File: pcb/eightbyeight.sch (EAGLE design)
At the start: 163 parts, among them J1 USB_MICROSMT+THRUHULE, J2 BATTERY, Q1 16MHz, SW1 SWITCH_SPDT, SW2 BRIGHTNESS, U1 MK20DN64VFM5, U10 FDG6316P, U11 FDG6316P, U12 FDG6316P, U2 ICN2026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

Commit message: Add HRC art
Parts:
- R28: value DNP -> 10k
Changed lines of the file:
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@@
 <part name="3V17" library="supply1" deviceset="+3V3" device=""/>
 <part name="3V18" library="supply1" deviceset="+3V3" device=""/>
-<part name="R28" library="adafruit" deviceset="R-US_" device="R0402" value="DNP"/>
+<part name="R28" library="adafruit" deviceset="R-US_" device="R0402" value="10k"/>
 <part name="3V1" library="supply1" deviceset="+3V3" device=""/>
 <part name="3V4" library="supply1" deviceset="+3V3" device=""/>
@@
 Revision E:
 -Implement more user friendly expansion pads for the ESP
+Revision F:
+-Round badge corners slightly
+-Increase base brightness for LED resistors
 TODO:
--Cosmetic: ESP8266 GPIO 18mislabeled, should be 16</text>
+-Cosmetic: ESP8266 GPIO 18mislabeled, should be 16
+-Clean silkscreen for final release</text>
 <text x="129.54" y="358.14" size="10.16" layer="91" align="bottom-center">EightByEight Blinky Badge</text>
 <text x="129.54" y="345.44" size="6.4516" layer="91" align="bottom-center">Copyright 2016 Blinkinlabs, LLC</text>

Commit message: Production silk and component values
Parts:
- R1: value 1.6k 1% -> 1k 1%
- R9: value 2k 1% -> 1k 1%
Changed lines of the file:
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@@
 <part name="GND2" library="SparkFun-Aesthetics" deviceset="GND" device=""/>
 <part name="C7" library="adafruit" deviceset="C-US" device="C0402" value="100nF"/>
-<part name="R1" library="adafruit" deviceset="R-US_" device="R0402" value="1.6k 1%"/>
+<part name="R1" library="adafruit" deviceset="R-US_" device="R0402" value="1k 1%"/>
 <part name="GND3" library="SparkFun-Aesthetics" deviceset="GND" device=""/>
 <part name="GND4" library="SparkFun-Aesthetics" deviceset="GND" device=""/>
@@
 <part name="U4" library="blinkinlabs" deviceset="ICN2026" device=""/>
 <part name="GND9" library="SparkFun-Aesthetics" deviceset="GND" device=""/>
-<part name="R9" library="adafruit" deviceset="R-US_" device="R0402" value="2k 1%"/>
+<part name="R9" library="adafruit" deviceset="R-US_" device="R0402" value="1k 1%"/>
 <part name="GND11" library="SparkFun-Aesthetics" deviceset="GND" device=""/>
 <part name="C11" library="adafruit" deviceset="C-US" device="C0402" value="100nF"/>
@@
 -Increase base brightness for LED resistors
 TODO:
--Cosmetic: ESP8266 GPIO 18mislabeled, should be 16
--Clean silkscreen for final release</text>
+-Cosmetic: ESP8266 GPIO 18mislabeled, should be 16</text>
 <text x="129.54" y="358.14" size="10.16" layer="91" align="bottom-center">EightByEight Blinky Badge</text>
 <text x="129.54" y="345.44" size="6.4516" layer="91" align="bottom-center">Copyright 2016 Blinkinlabs, LLC</text>

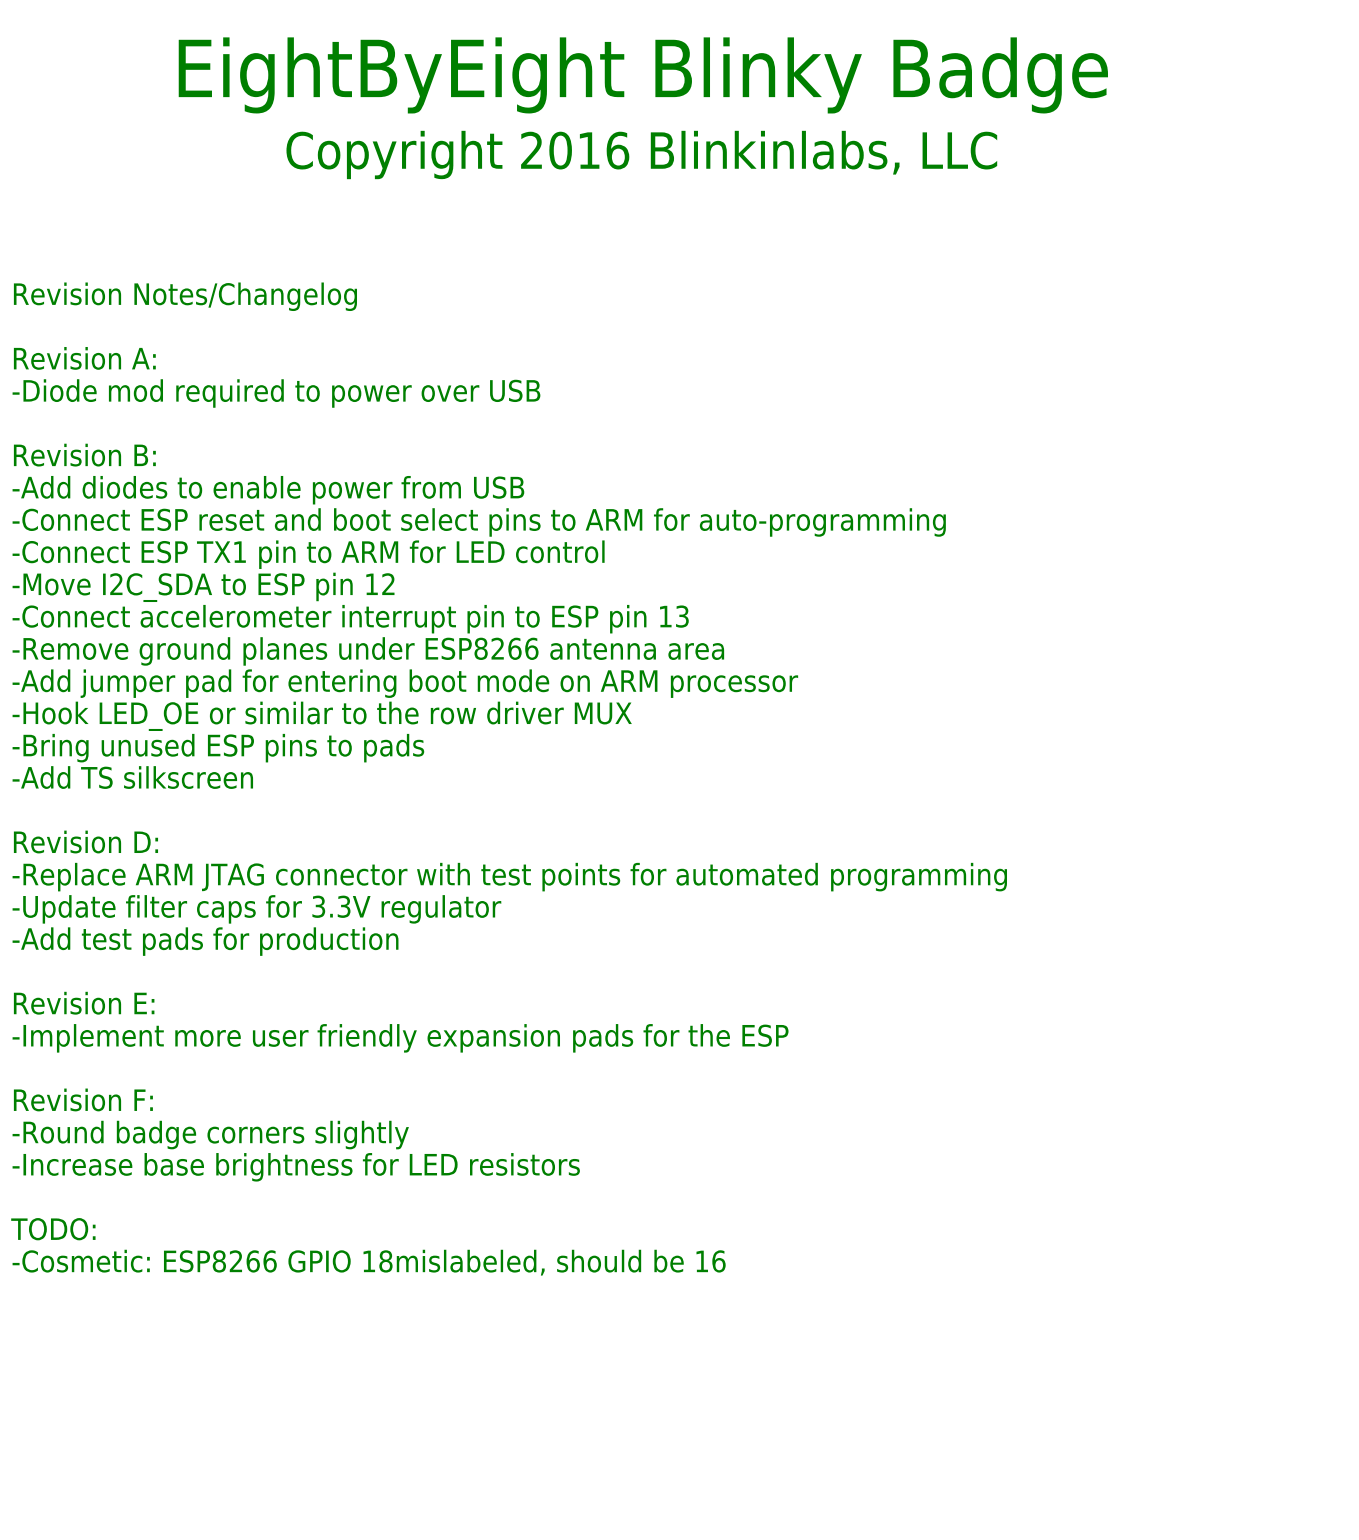
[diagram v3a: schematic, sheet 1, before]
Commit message: Add CERH OHL license to PCB
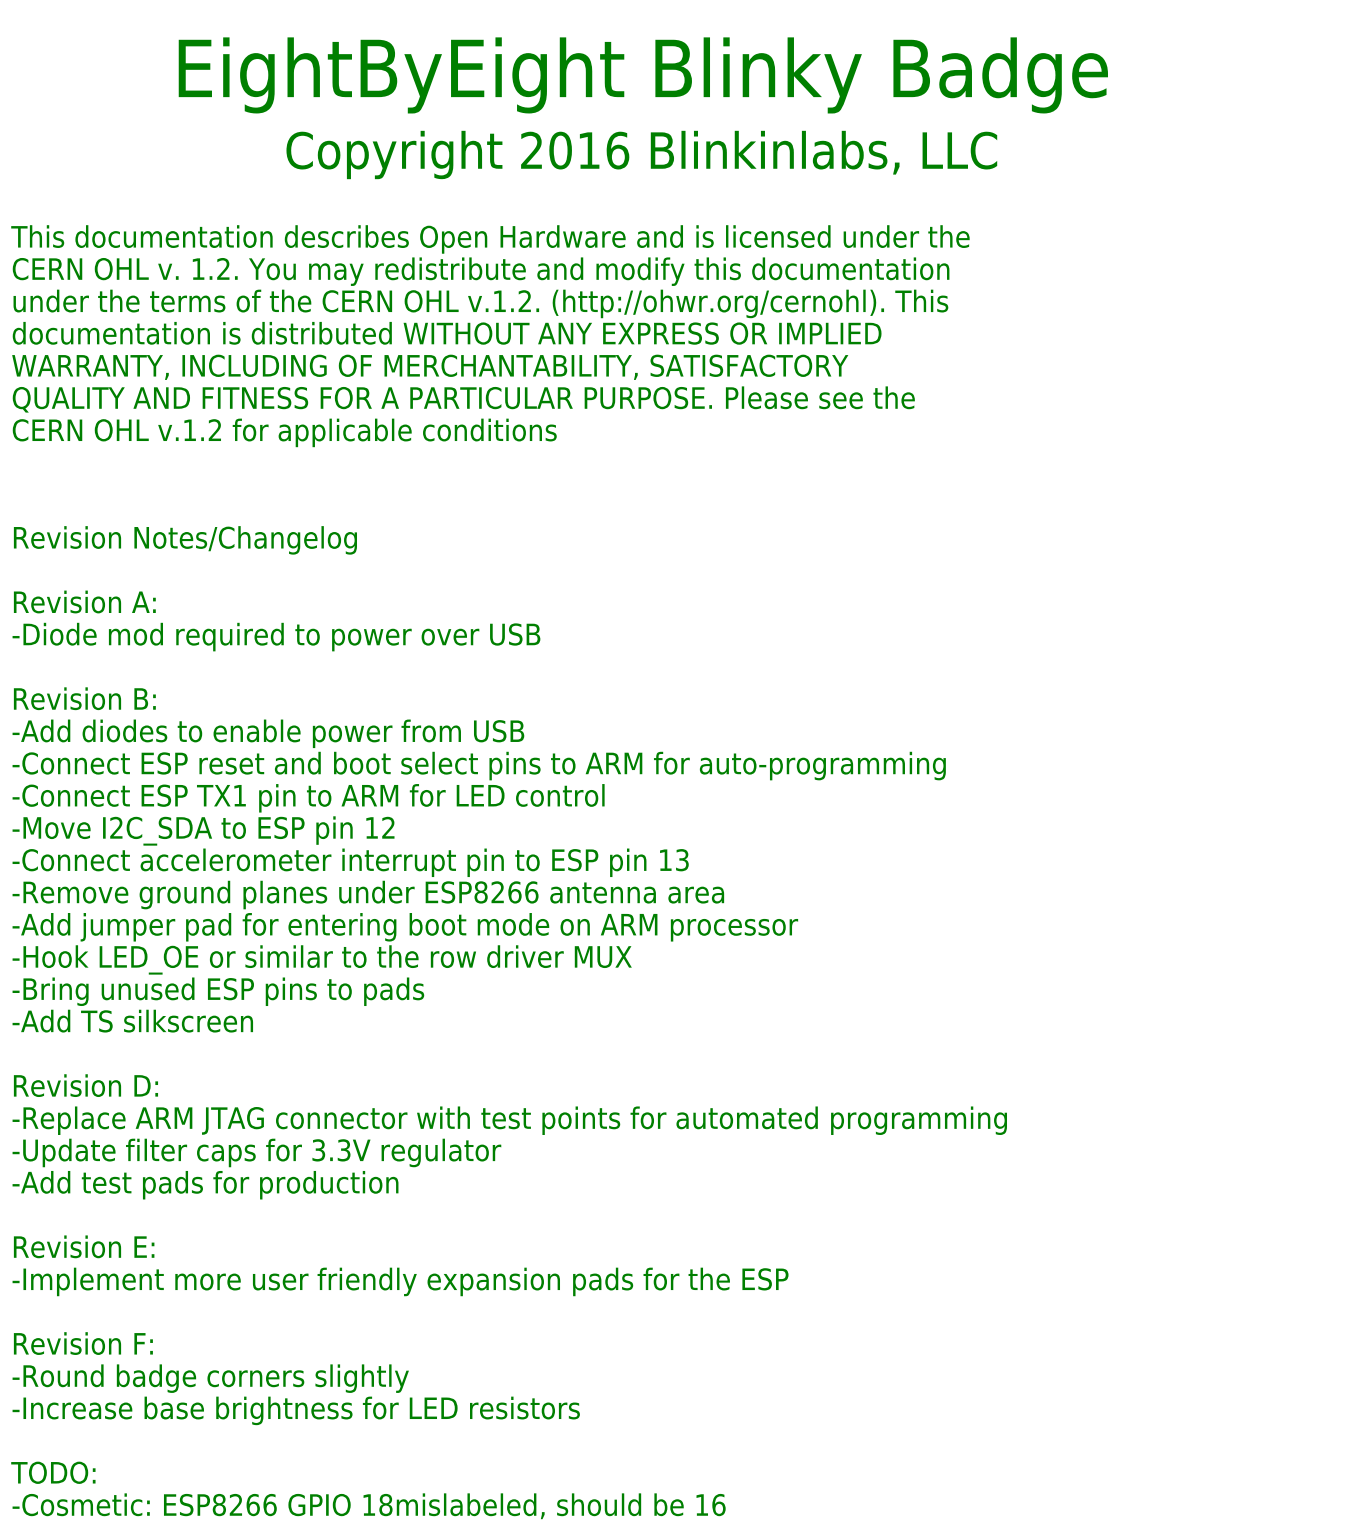
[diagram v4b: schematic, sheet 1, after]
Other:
- note added: "This documentation describes Open Hardware and is licensed under the CERN OHL v. 1.2. You may redistribute and modify this documentation under the terms of the CERN OHL v.1.2. (http://ohwr.org/cernohl). This documentation is distributed WITHOUT ANY EXPRESS OR IMPLIED WARRANTY, INCLUDING OF MERCHANTABILITY, SATISFACTORY QUALITY AND FITNESS FOR A PARTICULAR PURPOSE. Please see the CERN OHL v.1.2 fo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"
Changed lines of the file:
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@@
 <?xml version="1.0" encoding="utf-8"?>
 <!DOCTYPE eagle SYSTEM "eagle.dtd">
-<eagle version="7.6.0">
+<eagle version="7.5.0">
 <drawing>
 <settings>
@@
 <sheet>
 <plain>
-<text x="17.78" y="325.12" size="3.81" layer="91" align="top-left">Revision Notes/Changelog
+<text x="17.78" y="281.94" size="3.81" layer="91" align="top-left">Revision Notes/Changelog
 Revision A:
 -Diode mod required to power over USB
@@
 <text x="129.54" y="358.14" size="10.16" layer="91" align="bottom-center">EightByEight Blinky Badge</text>
 <text x="129.54" y="345.44" size="6.4516" layer="91" align="bottom-center">Copyright 2016 Blinkinlabs, LLC</text>
+<text x="17.78" y="297.18" size="3.81" layer="91">This documentation describes Open Hardware and is licensed under the
+CERN OHL v. 1.2. You may redistribute and modify this documentation
+under the terms of the CERN OHL v.1.2. (http://ohwr.org/cernohl). This
+documentation is distributed WITHOUT ANY EXPRESS OR IMPLIED
+WARRANTY, INCLUDING OF MERCHANTABILITY, SATISFACTORY
+QUALITY AND FITNESS FOR A PARTICULAR PURPOSE. Please see the
+CERN OHL v.1.2 for applicable conditions </text>
 </plain>
 <instances>

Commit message: Update board errata
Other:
- note added: "Pin assignments for matrix output: LED_DAT + LED_CLK use ESPI hardware LED_OE and LED_STB need to be on pins with FTM0 capability LED_ROW_* are GPIO and need to be together on a unique port"
- note removed: "Pin assignments for matrix output: LED_DAT + LED_CLK use ESPI hardware LED_OE needs to be on a pin with FTM capability LED_ROW_* and LED_STB are GPIO and need to be together on a unique port"
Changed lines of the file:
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@@
 <text x="76.2" y="101.6" size="1.778" layer="91">Pin assignments for matrix output:
 LED_DAT + LED_CLK use ESPI hardware
-LED_OE needs to be on a pin with FTM capability
-LED_ROW_* and LED_STB are GPIO and need to be together on a unique port</text>
+LED_OE and LED_STB need to be on pins with FTM0 capability
+LED_ROW_* are GPIO and need to be together on a unique port</text>
 <text x="12.7" y="238.76" size="1.778" layer="91">Provides LED drive signal, USB/Serial conversion</text>
 <text x="12.7" y="243.84" size="2.54" layer="94">ARM microcontroller</text>
